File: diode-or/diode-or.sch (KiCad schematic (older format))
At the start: 23 parts, among them J1 Conn_01x01, J2 Conn_01x01, J3 Conn_01x01, J4 Conn_01x01, J5 Conn_01x01, Q1 Q_NMOS_GDS, SW1 SW_SPDT, U1 LM5050-1

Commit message: Routed diode-or board. Add generated files.
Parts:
- added H1, H2, H3, H4: MountingHole_Pad, MountingHole:MountingHole_3.2mm_M3_Pad_Via, symbol Mechanical:MountingHole_Pad
- added HS1: Heatsink_Pad, local:MA-301-27E, symbol Mechanical:Heatsink_Pad
- C1: footprint local:C_1206_HandSoldering -> Capacitor_SMD:CP_Elec_6.3x5.9; symbol Device:C -> Device:CP1; Dielectric X7R -> Poly; Manufacturer Kemet -> Panasonic; PartNum C0805C104K5RACTU -> 50SVPK22M; Tolerance 10% -> 20%
- C3: value 10uF -> 1uF; Manufacturer Kemet -> ‎Samsung; PartNum C0805C104K5RACTU -> CL31B105KCHNFNE; Voltage 50V -> 100V
- D1: Current (none) -> 20A; Manufacturer (none) -> STMicro; PartNum (none) -> STPS40H100CW; Voltage (none) -> 100V
- D2: Manufacturer (none) -> ‎Littelfuse; PartNum (none) -> SMBJ60A; Voltage (none) -> 60V
- D4, D6: Current (none) -> 1A; Manufacturer (none) -> ON Semiconductor‎; PartNum (none) -> SS16T3; Voltage (none) -> 60V
- D7: value D_Zener -> MM3Z4V3T1G; footprint Diode_SMD:D_0805_2012Metric -> local:SOD-323_477-02-H_HandSoldering; Manufacturer (none) -> ON Semiconductor; PartNum (none) -> MM3Z4V3T1G; Power (none) -> 300mW; Voltage 4.0V -> 4.3V
- D8: Manufacturer (none) -> Kingbright; PartNum (none) -> AM2520ZGC09
- J1, J2, J3: value Conn_01x01 -> Binding Post (RED); Manufacturer (none) -> Keystone; PartNum (none) -> 7016
- J4, J5: value Conn_01x01 -> Binding Post (BLACK); Manufacturer (none) -> Keystone; PartNum (none) -> 7017
- Q1: value Q_NMOS_GDS -> IRFP4710PBF; Current (none) -> 72A; Manufacturer (none) -> Infineon; PartNum (none) -> IRFP4710PBF; Power (none) -> 190W; Voltage (none) -> 100V
- SW1: footprint Button_Switch_THT:SW_CuK_OS102011MA1QN1_SPDT_Angled -> local:ASE1D-2M-10-Z; Current (none) -> 50mA; Manufacturer (none) -> Nidec Copal; PartNum (none) -> ASE1D-2M-10-Z; Voltage (none) -> 60V
- U1: footprint Package_TO_SOT_SMD:TSOT-23-6_HandSoldering -> Package_TO_SOT_SMD:TSOT-23-6; Manufacturer (none) -> Texas Instruments; PartNum (none) -> LM5050MKX-1
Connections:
- net IN_OUT_N: now also H1.1, H2.1, H3.1, H4.1, HS1.1
- no-connect marks 0 -> 1
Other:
- moved on the sheet: J3, J4

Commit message: Use a current source to drive the LED indicator. Update footprints in the diode-or board.
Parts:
- added U2: PSSI2021SAY, Package_TO_SOT_SMD:SOT-353_SC-70-5, symbol Local:PSSI2021SAY
- C3: Manufacturer ‎Samsung -> Samsung
- D2: Manufacturer ‎Littelfuse -> Littelfuse
- D4, D6: Manufacturer ON Semiconductor‎ -> ON Semiconductor
- HS1: value Heatsink_Pad -> MA-301-27E; Manufacturer (none) -> Ohmite; PartNum (none) -> MA-301-27E
- R3: value 14.0K -> 634; PartNum CRCW080514K0FKEA -> CRCW080634R0FKEA
- SW1: footprint local:ASE1D-2M-10-Z -> local:ASE1D-6M-10-Z
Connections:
- net GND: now also U2.3 (GND)
- net VS: now also U2.5 (VS)
- net VS_OR: now also SW1.1 (A); no longer SW1.3 (C)
- net IOUT: now reaches D7.1 (K)
- net IOUT: now also U2.2 (IOUT); no longer R3.2
- new net REXT: R3.2, U2.4 (REXT)
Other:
- moved on the sheet: D3, D5, D7, D8, R1, R2, R3

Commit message: Fix resistor part number. Clean up position of text on the Fab layers.
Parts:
- R3: PartNum CRCW080634R0FKEA -> CRCW0805634RFKEA
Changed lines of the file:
@@
 F 5 "0.125W" V 5375 5650 50  0000 C CNN "Power"
 F 6 "Vishay Dale" V 5600 5650 50  0001 C CNN "Manufacturer"
-F 7 "CRCW080634R0FKEA" V 5750 5650 50  0001 C CNN "PartNum"
+F 7 "CRCW0805634RFKEA" V 5750 5650 50  0001 C CNN "PartNum"
 	1    5600 5650
 	1    0    0    -1

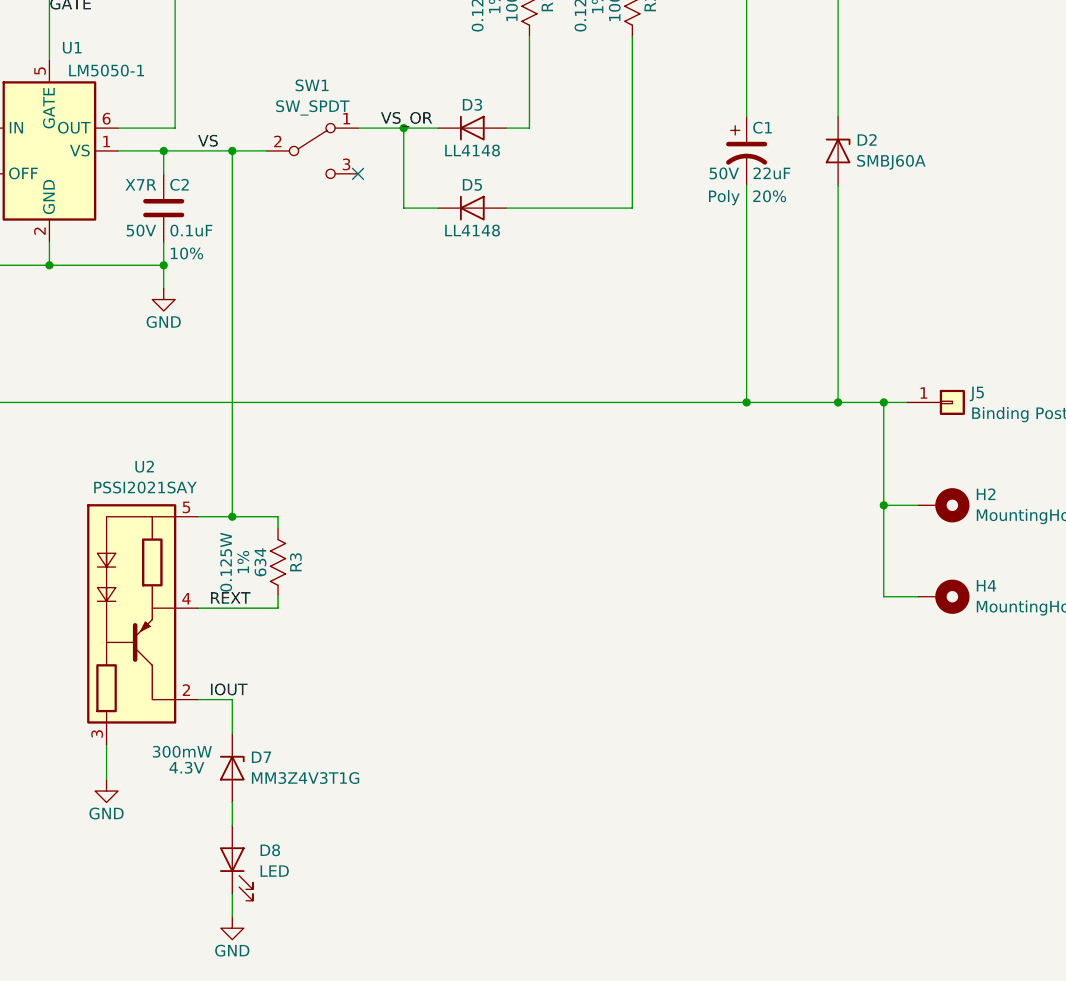
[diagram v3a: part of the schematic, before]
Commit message: Minor change to fill zones. Upload to OSHPark.
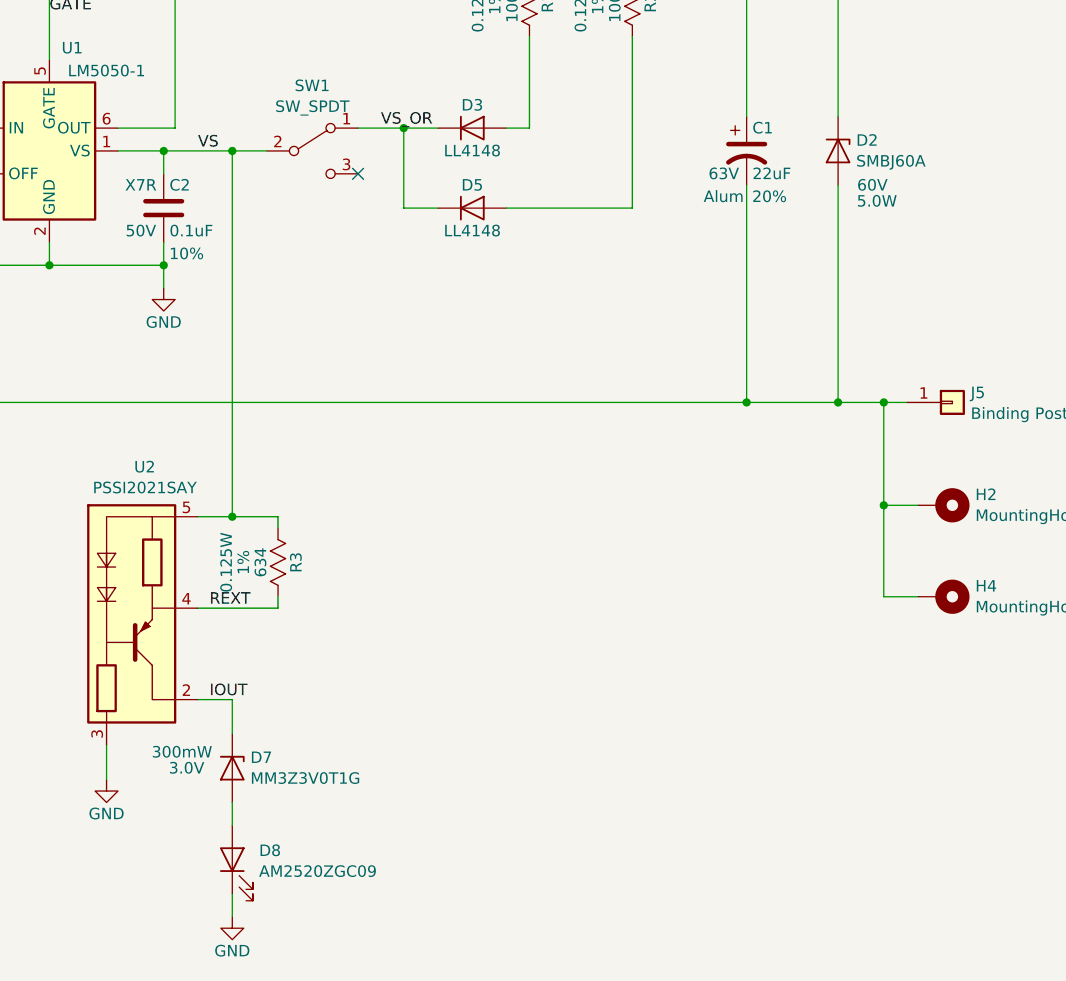
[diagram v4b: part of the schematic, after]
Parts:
- C1: Dielectric Poly -> Alum; PartNum 50SVPK22M -> EEE-FK1J220XP; Voltage 50V -> 63V
- D2: Power (none) -> 5.0W
- D7: value MM3Z4V3T1G -> MM3Z3V0T1G; PartNum MM3Z4V3T1G -> MM3Z3V0T1G; Voltage 4.3V -> 3.0V
- D8: value LED -> AM2520ZGC09
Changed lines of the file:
@@
 F 4 "Littelfuse" H 8050 3850 50  0001 C CNN "Manufacturer"
 F 5 "SMBJ60A" H 8050 3850 50  0001 C CNN "PartNum"
-F 6 "60V" H 8050 3850 50  0001 C CNN "Voltage"
+F 6 "60V" V 8200 4000 50  0000 C CNN "Voltage"
+F 7 "5.0W" V 8270 4020 50  0000 C CNN "Power"
 	1    8050 3850
 	0    1    1    0
@@
 F 2 "Capacitor_SMD:CP_Elec_6.3x5.9" H 7688 3700 30  0001 C CNN
 F 3 "" H 7650 3850 60  0000 C CNN
-F 4 "50V" H 7550 3750 50  0000 C CNN "Voltage"
+F 4 "63V" H 7550 3750 50  0000 C CNN "Voltage"
 F 5 "20%" H 7750 3650 50  0000 C CNN "Tolerance"
-F 6 "Poly" H 7550 3650 50  0000 C CNN "Dielectric"
+F 6 "Alum" H 7550 3650 50  0000 C CNN "Dielectric"
 F 7 "Panasonic" H 7650 3850 50  0001 C CNN "Manufacturer"
-F 8 "50SVPK22M" H 7650 3850 50  0001 C CNN "PartNum"
+F 8 "EEE-FK1J220XP" H 7650 3850 50  0001 C CNN "PartNum"
 	1    7650 3850
 	1    0    0    -1
@@
 P 5400 6950
 F 0 "D8" V 5439 6833 50  0000 R CNN
-F 1 "LED" V 5348 6833 50  0000 R CNN
+F 1 "AM2520ZGC09" V 5348 6833 50  0000 R CNN
 F 2 "local:AM2520ZGC09" H 5400 6950 50  0001 C CNN
 F 3 "~" H 5400 6950 50  0001 C CNN
@@
 P 5400 6550
 F 0 "D7" V 5354 6629 50  0000 L CNN
-F 1 "MM3Z4V3T1G" V 5445 6629 50  0000 L CNN
+F 1 "MM3Z3V0T1G" V 5445 6629 50  0000 L CNN
 F 2 "local:SOD-323_477-02-H_HandSoldering" H 5400 6550 50  0001 C CNN
 F 3 "~" H 5400 6550 50  0001 C CNN
-F 4 "4.3V" V 5400 6350 50  0000 C CNN "Voltage"
+F 4 "3.0V" V 5400 6350 50  0000 C CNN "Voltage"
 F 5 "ON Semiconductor" H 5400 6550 50  0001 C CNN "Manufacturer"
-F 6 "MM3Z4V3T1G" H 5400 6550 50  0001 C CNN "PartNum"
+F 6 "MM3Z3V0T1G" H 5400 6550 50  0001 C CNN "PartNum"
 F 7 "300mW" V 5330 6330 50  0000 C CNN "Power"
 	1    5400 6550

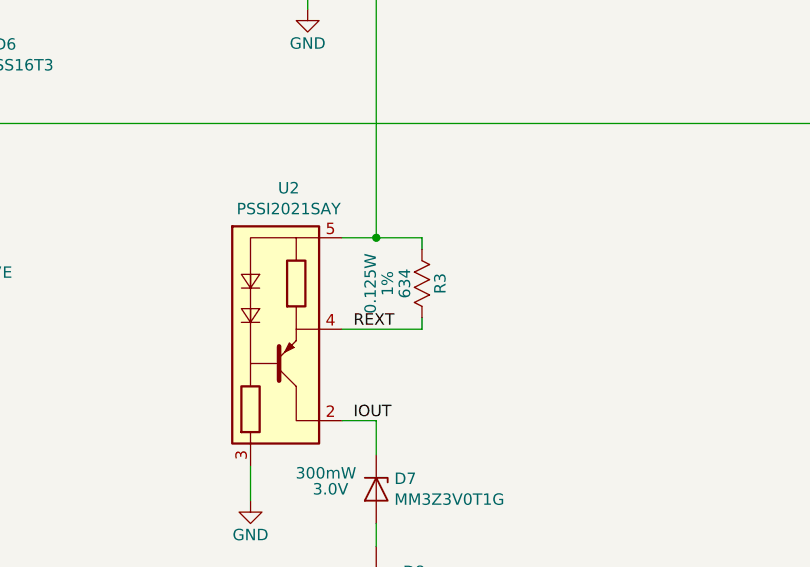
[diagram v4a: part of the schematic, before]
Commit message: Change current source resistor value to 4.99k
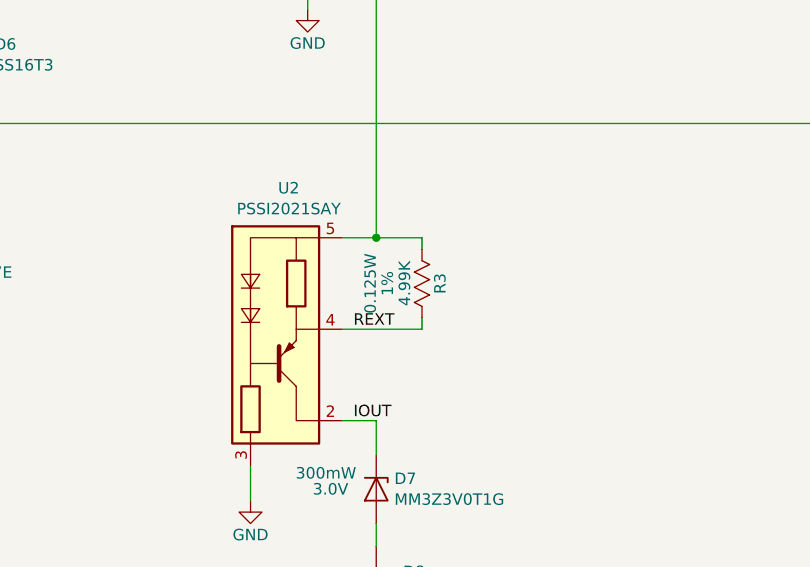
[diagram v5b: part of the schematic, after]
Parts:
- R3: value 634 -> 4.99K; PartNum CRCW0805634RFKEA -> CRCW08054K99FKEA
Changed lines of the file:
@@
 Sheet 1 1
 Title "Diode - ORing"
-Date "2020-01-07"
-Rev "v1.0.0"
+Date "2020-01-31"
+Rev "v1.0.1"
 Comp ""
 Comment1 ""
@@
 P 5600 5650
 F 0 "R3" V 5680 5650 50  0000 C CNN
-F 1 "634" V 5525 5650 50  0000 C CNN
+F 1 "4.99K" V 5525 5650 50  0000 C CNN
 F 2 "local:R_0805_HandSoldering" V 5530 5650 30  0001 C CNN
 F 3 "" V 5680 5650 30  0000 C CNN
@@
 F 5 "0.125W" V 5375 5650 50  0000 C CNN "Power"
 F 6 "Vishay Dale" V 5600 5650 50  0001 C CNN "Manufacturer"
-F 7 "CRCW0805634RFKEA" V 5750 5650 50  0001 C CNN "PartNum"
+F 7 "CRCW08054K99FKEA" V 5750 5650 50  0001 C CNN "PartNum"
 	1    5600 5650
 	1    0    0    -1
